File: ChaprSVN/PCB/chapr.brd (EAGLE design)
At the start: 68.6 x 55.6 mm, 30 parts, among them M2 RN42 Module, T1 3906, T2 3904

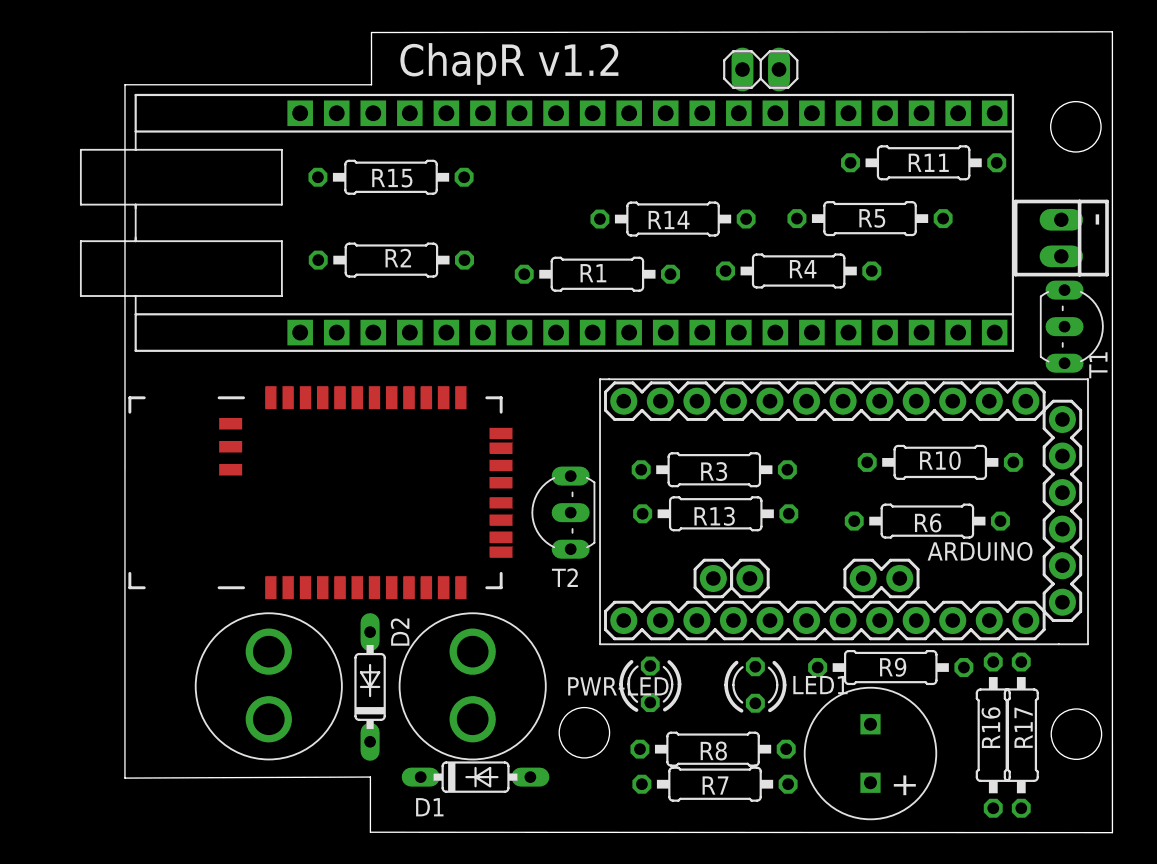
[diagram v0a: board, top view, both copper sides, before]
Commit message: 
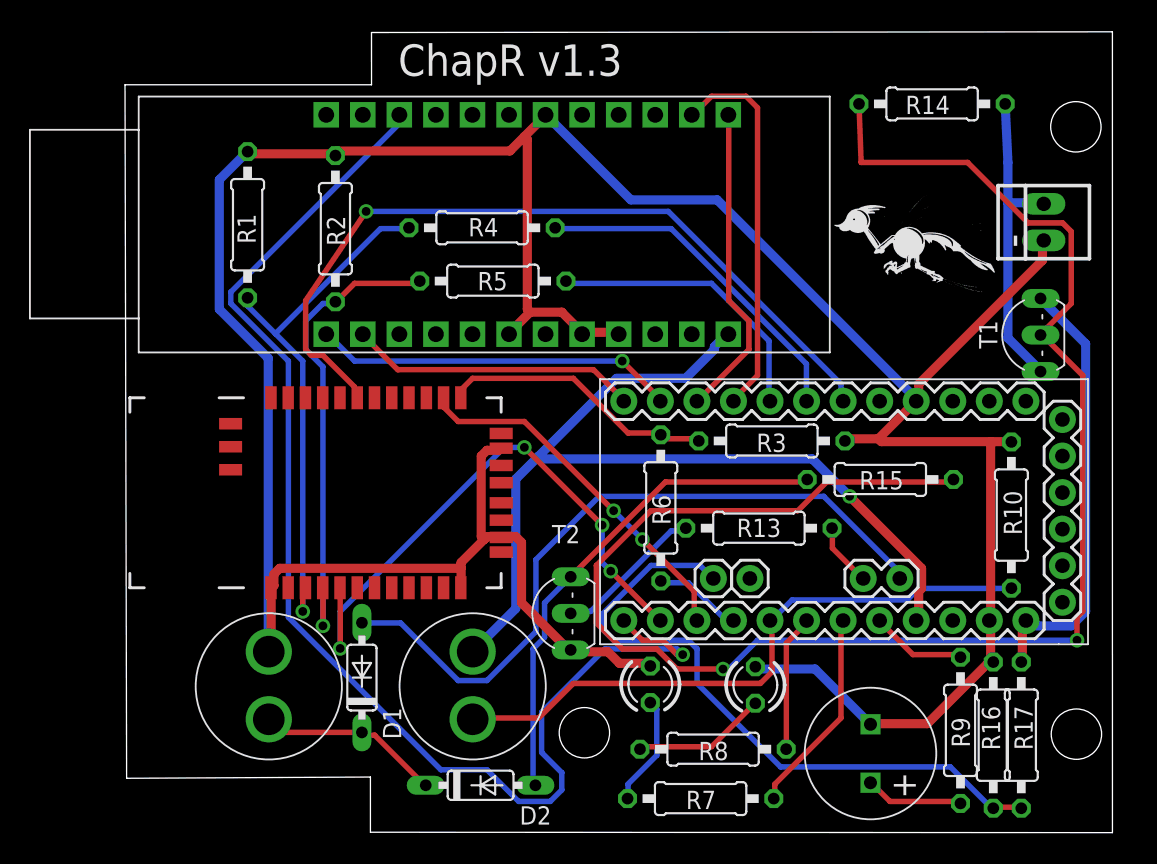
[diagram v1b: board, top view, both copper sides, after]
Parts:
- removed JP1: (no value), pinhead:1X02
- removed R11: 10k, resistor:0207/10
- removed U$3: VDIP2BIGHOLE, ChapR-Custom:VDIP2-BIGHOLE
- added V2DIP2: V2DIP2, ChapR-Custom:V2DIP2
- moved R15 40.0 mm to (54.5, 25.2)
- moved R5 26.6 mm to (27.6, 39.0)
- moved R1 24.5 mm to (10.6, 42.9), turned to 270 degrees
- moved R4 22.2 mm to (26.9, 42.7)
- moved R14 19.7 mm to (58.1, 51.3)
- moved R6 18.5 mm to (39.3, 23.2), turned to 270 degrees
- moved D1 10.5 mm to (18.5, 11.4), turned to 90 degrees
- moved D2 10.3 mm to (26.8, 3.92), turned to 0 degrees
- moved T2 7.00 mm to (31.7, 15.9)
- moved R9 6.52 mm to (60.1, 7.74), turned to 90 degrees
- moved R10 6.15 mm to (63.6, 22.7), turned to 270 degrees
- moved R3 4.47 mm to (47.0, 27.8)
- moved R2 4.46 mm to (16.7, 42.6), turned to 270 degrees
- moved T1 4.25 mm to (64.4, 35.2), turned to 90 degrees
- moved R13 3.16 mm to (46.1, 21.8)
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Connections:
- removed net LED1(BD5): U$3.4
- removed net LED2(BD6): U$3.5
- removed net N$22: JP1.1, M2.22, R11.2
- removed net NC(1): U$3.1
- removed net NC(2): U$3.40
- new net N$28: V2DIP2.P$24
- net +3V3: no longer JP1.2, U$3.32, U$3.38, U$3.39
- net +5V: now also V2DIP2.P$1; no longer U$3.2, U$3.3, U$3.9
- net GND: now also V2DIP2.P$18, V2DIP2.P$4, V2DIP2.P$5, V2DIP2.P$7; no longer R11.1, U$3.12, U$3.13, U$3.15, U$3.26
- net N$10: now also ARDUINO.D6, V2DIP2.P$14; no longer ARDUINO.D9, U$3.18
- net N$11: now also ARDUINO.D7, V2DIP2.P$13; no longer ARDUINO.D8, U$3.17
- net N$12: now also ARDUINO.D8, V2DIP2.P$12; no longer ARDUINO.D7, U$3.16
- net N$13: now also ARDUINO.D9, V2DIP2.P$11; no longer ARDUINO.D6, U$3.14
- net N$2: now also V2DIP2.P$22; no longer U$3.30
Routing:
- net GND: track 0.00 -> 228.4 mm
- net N$1: track 0.00 -> 118.3 mm, vias 0 -> 2
- net N$2: track 0.00 -> 88.9 mm, vias 0 -> 1
- net +5V: track 0.00 -> 66.0 mm, vias 0 -> 1
- net N$15: track 0.00 -> 55.4 mm, vias 0 -> 1
- net N$29: track 0.00 -> 49.9 mm
- net N$31: track 0.00 -> 46.3 mm
- net N$24: track 0.00 -> 43.4 mm
- net N$5: track 0.00 -> 40.3 mm, vias 0 -> 4
- net N$6: track 0.00 -> 37.5 mm, vias 0 -> 1
- net N$25: track 0.00 -> 35.0 mm
- net N$7: track 0.00 -> 33.4 mm, vias 0 -> 1
- net N$23: track 0.00 -> 30.8 mm
- net N$10: track 0.00 -> 26.5 mm
- net N$4: track 0.00 -> 25.5 mm, vias 0 -> 2
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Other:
- outline, holes or cut-outs redrawn
- board text added: "ChapR v1.3"
- board text removed: "ChapR v1.2"

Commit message: 
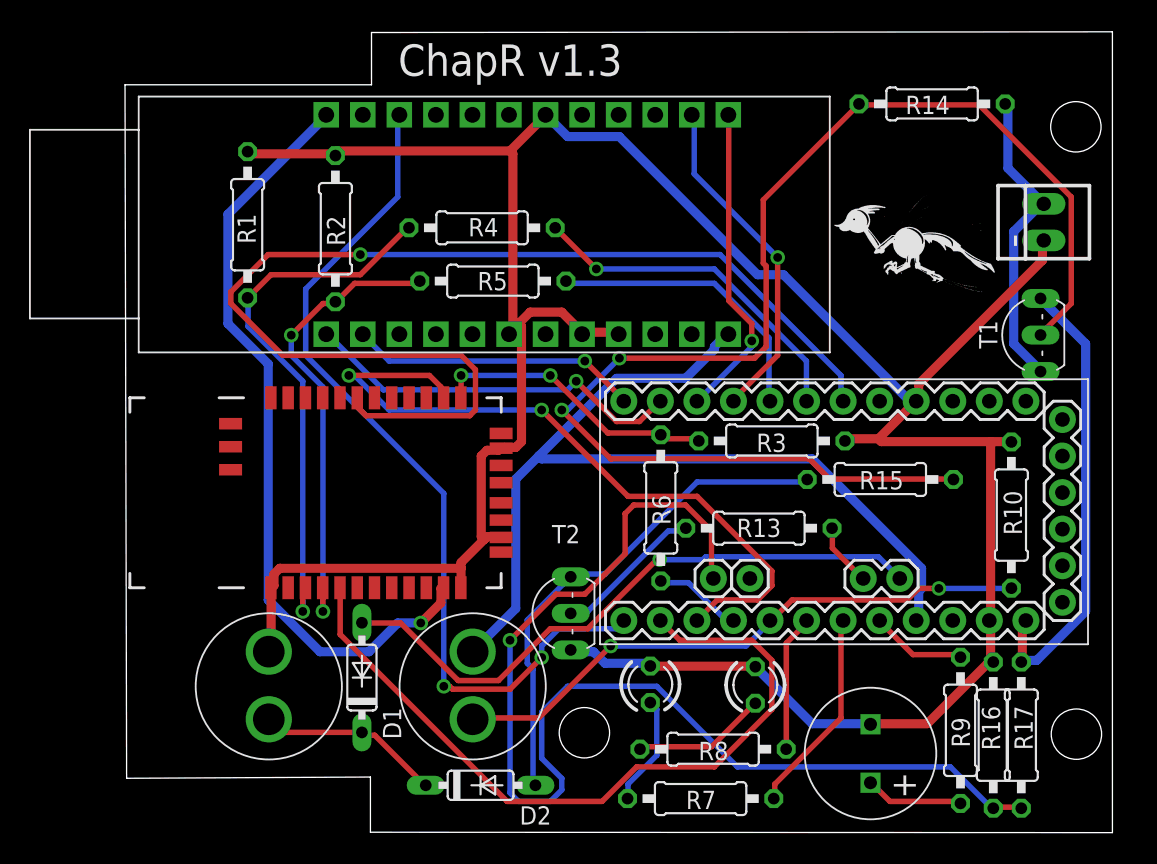
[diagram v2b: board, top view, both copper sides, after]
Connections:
- removed net N$28: V2DIP2.P$24
- net +3V3: now also V2DIP2.P$24
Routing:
- net +3V3: track 0.00 -> 53.8 mm, vias 0 -> 1
- net N$31: track 46.3 -> 82.1 mm, vias 0 -> 1
- net GND: track 228.4 -> 199.3 mm
- net N$2: track 88.9 -> 61.4 mm, vias 1 -> 2
- net N$1: track 118.3 -> 92.8 mm
- net N$15: track 55.4 -> 80.6 mm
- net N$4: track 25.5 -> 49.8 mm
- net N$5: track 40.3 -> 53.0 mm, vias 4 -> 0
- net N$29: track 49.9 -> 43.2 mm, vias 0 -> 1
- net N$10: track 26.5 -> 23.7 mm, vias 0 -> 1
- net N$24: track 43.4 -> 41.2 mm, vias 0 -> 2
- net N$12: track 25.2 -> 26.8 mm
- net N$23: track 30.8 -> 32.0 mm
- net N$7: track 33.4 -> 32.3 mm, vias 1 -> 2
- net N$6: track 37.5 -> 38.4 mm
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
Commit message: Used the new ProMini without the top 6 pins. Created AutoRouter and DesignRule files for repeatable routing. Added clearance between vias and pads so we don't have to post-process the routes.
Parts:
- ARDUINO: value PROMINI -> PROMININOHEADER; device ChapR-Custom:PROMINI -> ChapR-Custom:PROMININOHEADER
- moved T1 2.51 mm to (66.7, 36.1), turned to 270 degrees
- moved D1 2.06 mm to (20.2, 10.3)
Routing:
- net N$1: track 92.8 -> 36.9 mm, vias 2 -> 0
- net N$31: track 82.1 -> 44.8 mm
- net N$2: track 61.4 -> 92.5 mm, vias 2 -> 1
- net N$15: track 80.6 -> 54.6 mm, vias 1 -> 0
- net N$5: track 53.0 -> 28.1 mm, vias 0 -> 2
- net N$4: track 49.8 -> 35.1 mm, vias 2 -> 1
- net N$12: track 26.8 -> 39.7 mm, vias 1 -> 0
- net GND: track 199.3 -> 188.3 mm, vias 0 -> 1
- net N$24: track 41.2 -> 51.2 mm, vias 2 -> 0
- net N$23: track 32.0 -> 22.1 mm
- net +9V: track 21.6 -> 15.7 mm
- net +5V: track 66.0 -> 62.5 mm
- net N$10: track 23.7 -> 26.6 mm, vias 1 -> 0
- net +3V3: track 53.8 -> 52.9 mm
- net N$6: track 38.4 -> 37.6 mm
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
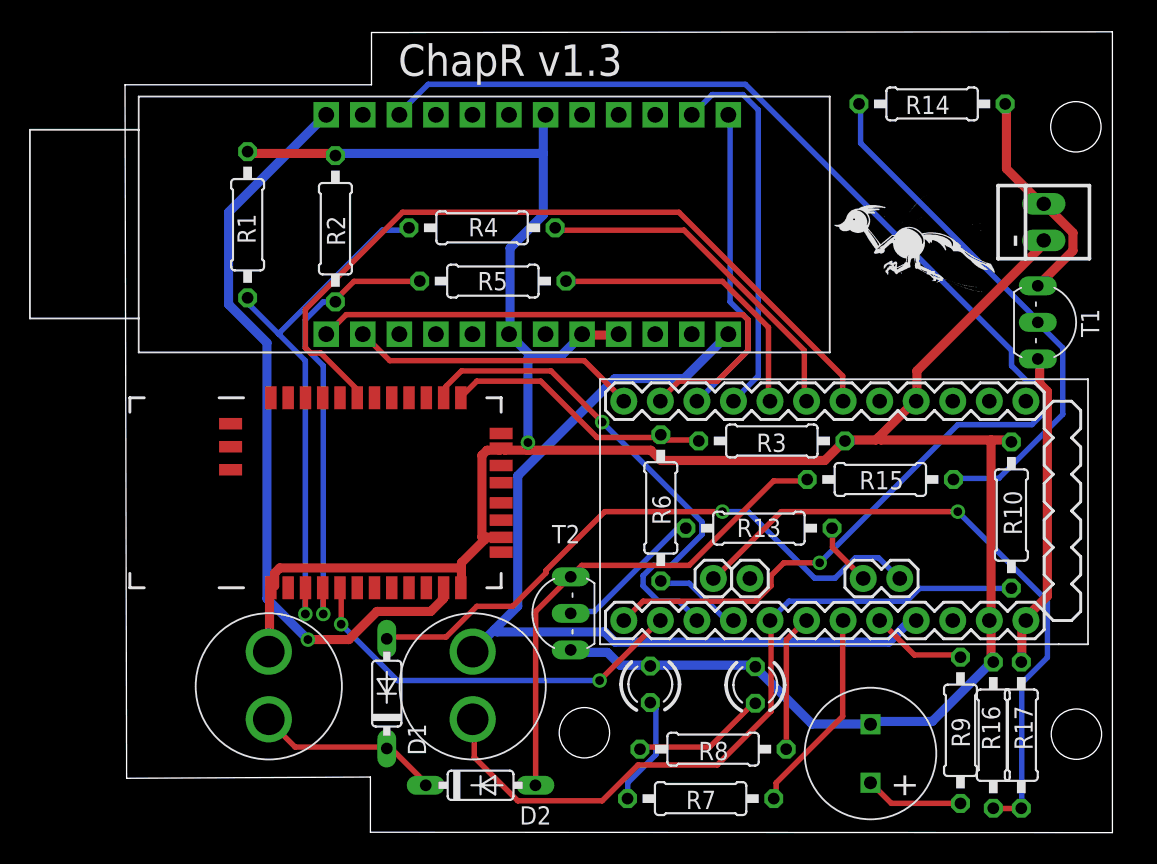
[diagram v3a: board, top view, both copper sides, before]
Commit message: 
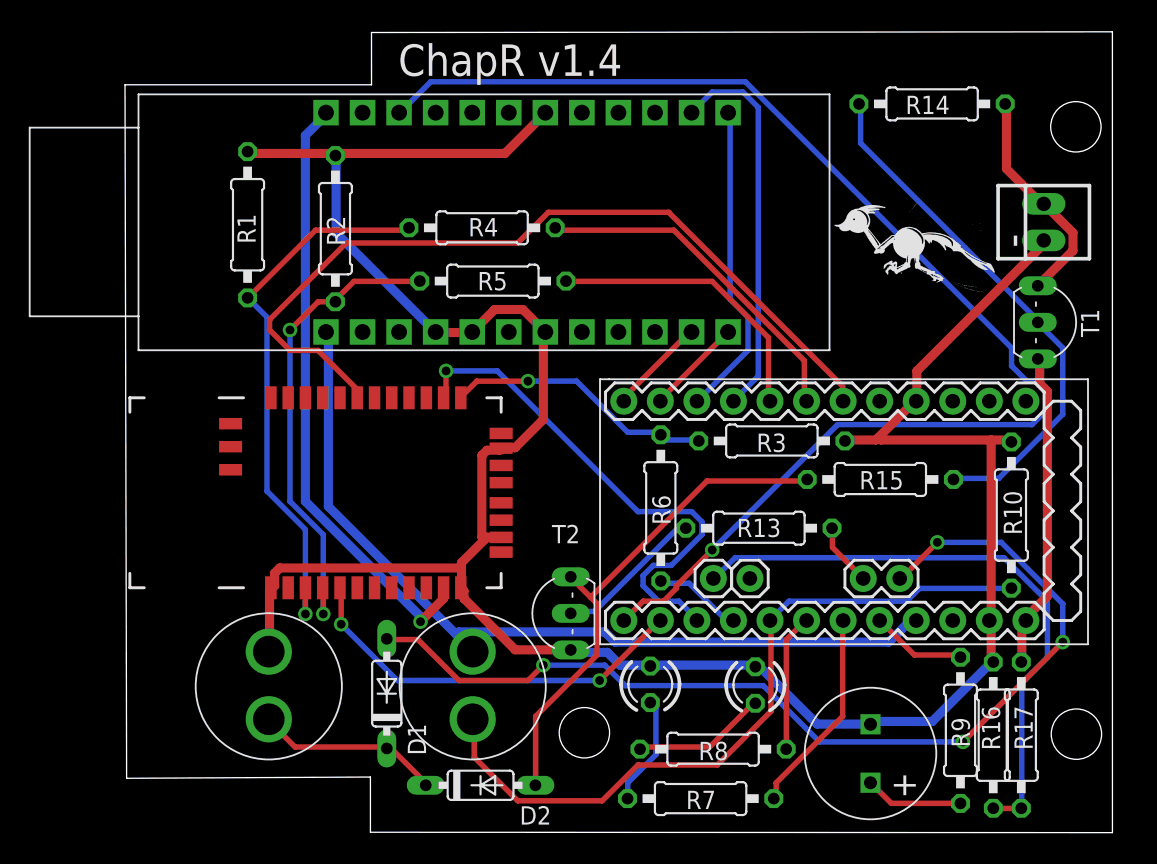
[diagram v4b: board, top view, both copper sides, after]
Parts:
- removed V2DIP2: V2DIP2, ChapR-Custom:V2DIP2
- added U$1: V2DIP2, ChapR-Custom:V2DIP2
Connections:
- net +3V3: now also U$1.P$24; no longer V2DIP2.P$24
- net +5V: now also U$1.P$1; no longer V2DIP2.P$1
- net GND: now also U$1.P$18, U$1.P$4, U$1.P$5, U$1.P$7; no longer V2DIP2.P$18, V2DIP2.P$4, V2DIP2.P$5, V2DIP2.P$7
- net N$10: now also U$1.P$14; no longer V2DIP2.P$14
- net N$11: now also U$1.P$13; no longer V2DIP2.P$13
- net N$12: now also U$1.P$12; no longer V2DIP2.P$12
- net N$13: now also U$1.P$11; no longer V2DIP2.P$11
- net N$2: now also U$1.P$22; no longer V2DIP2.P$22
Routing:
- net N$12: track 39.7 -> 6.75 mm
- net N$29: track 42.6 -> 70.5 mm, vias 1 -> 4
- net N$13: track 20.1 -> 6.88 mm
- net GND: track 188.3 -> 176.7 mm, vias 1 -> 0
- net +3V3: track 52.9 -> 42.3 mm
- net N$15: track 54.6 -> 58.1 mm
- net +5V: track 62.5 -> 59.4 mm
- net N$31: track 44.8 -> 42.1 mm, vias 1 -> 0
- net N$6: track 37.6 -> 38.7 mm
- net N$7: track 31.9 -> 33.0 mm, vias 1 -> 2
- net N$9: track 19.6 -> 18.8 mm, vias 0 -> 1
- net N$25: track 34.8 -> 35.5 mm
- net N$4: track 35.1 -> 35.8 mm
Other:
- board text added: "ChapR v1.4"
- board text removed: "ChapR v1.3"
